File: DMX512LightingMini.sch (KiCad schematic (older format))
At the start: 1 part

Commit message: * 部品配置開始
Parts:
- added C? (x2): C, symbol C
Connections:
- net GND: now reaches IC?.5 (GND)
- net at IC?.6 (A): now also C?.1
- net at IC?.7 (B): now also C?.1
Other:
- moved on the sheet: IC?
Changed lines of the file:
@@
 LIBS:valves
 LIBS:SamacSys_Parts
+LIBS:DMX512LightingMini-cache
 EELAYER 25 0
 EELAYER END
@@
 L ADM4852ARZ-REEL7 IC?
 U 1 1 599C318A
-P 5150 3900
-F 0 "IC?" H 5600 4050 50  0000 C CNN
-F 1 "ADM4852ARZ-REEL7" H 5600 3450 50  0000 C CNN
-F 2 "SOIC127P600X175-8N" H 5600 3350 50  0001 C CNN
-F 3 "" H 5600 3250 50  0001 C CNN
-F 4 "Transceivers" H 5600 3150 50  0001 C CNN "Description"
-F 5 "RS" H 5600 3050 50  0001 C CNN "Supplier_Name"
-F 6 "" H 5600 2950 50  0001 C CNN "RS Part Number"
-F 7 "Analog Devices" H 5600 2850 50  0001 C CNN "Manufacturer_Name"
-F 8 "ADM4852ARZ-REEL7" H 5600 2750 50  0001 C CNN "Manufacturer_Part_Number"
-F 9 "" H 5600 2650 50  0001 C CNN "Allied_Number"
-F 10 "" H 5600 2550 50  0001 C CNN "Other Part Number"
-F 11 "" H 5900 2450 50  0001 C CNN "Height"
-	1    5150 3900
-	1    0    0    -1
+P 5400 3950
+F 0 "IC?" H 5850 4100 50  0000 C CNN
+F 1 "ADM4852ARZ-REEL7" H 5850 3500 50  0000 C CNN
+F 2 "SOIC127P600X175-8N" H 5850 3400 50  0001 C CNN
+F 3 "" H 5850 3300 50  0001 C CNN
+F 4 "Transceivers" H 5850 3200 50  0001 C CNN "Description"
+F 5 "RS" H 5850 3100 50  0001 C CNN "Supplier_Name"
+F 6 "Analog Devices" H 5850 2900 50  0001 C CNN "Manufacturer_Name"
+F 7 "ADM4852ARZ-REEL7" H 5850 2800 50  0001 C CNN "Manufacturer_Part_Number"
+	1    5400 3950
+	-1   0    0    -1
 $EndComp
+$Comp
+L C C?
+U 1 1 599C34D2
+P 3500 4050
+F 0 "C?" H 3525 4150 50  0000 L CNN
+F 1 "C" H 3525 3950 50  0000 L CNN
+F 2 "" H 3538 3900 50  0001 C CNN
+F 3 "" H 3500 4050 50  0001 C CNN
+	1    3500 4050
+	0    1    1    0
+$EndComp
+$Comp
+L C C?
+U 1 1 599C360D
+P 3500 4300
+F 0 "C?" H 3525 4400 50  0000 L CNN
+F 1 "C" H 3525 4200 50  0000 L CNN
+F 2 "" H 3538 4150 50  0001 C CNN
+F 3 "" H 3500 4300 50  0001 C CNN
+	1    3500 4300
+	0    1    1    0
+$EndComp
+$Comp
+L GND #PWR?
+U 1 1 599C37CE
+P 4450 3950
+F 0 "#PWR?" H 4450 3700 50  0001 C CNN
+F 1 "GND" H 4450 3800 50  0000 C CNN
+F 2 "" H 4450 3950 50  0001 C CNN
+F 3 "" H 4450 3950 50  0001 C CNN
+	1    4450 3950
+	0    1    1    0
+$EndComp
+Wire Wire Line
+	4450 3950 4500 3950
+Wire Wire Line
+	4500 4050 3650 4050
+Wire Wire Line
+	3650 4300 3750 4300
+Wire Wire Line
+	3750 4300 3750 4150
+Wire Wire Line
+	3750 4150 4500 4150
 $EndSCHEMATC

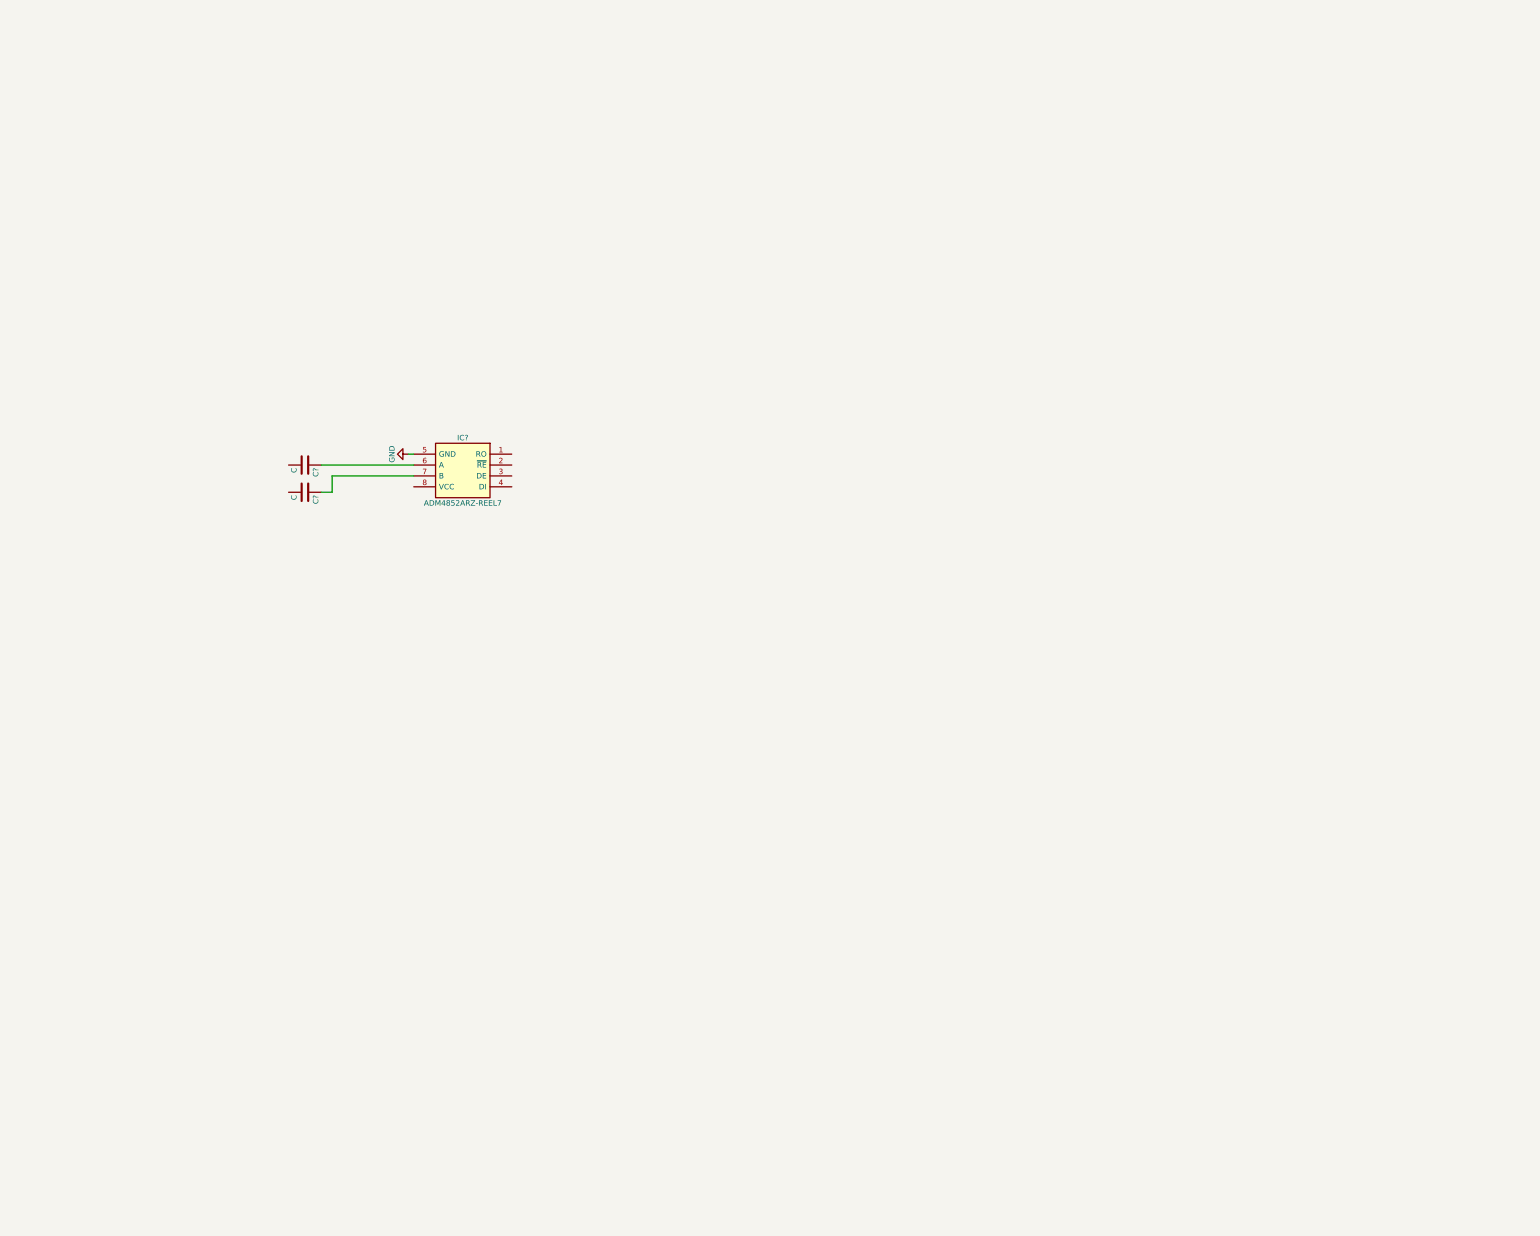
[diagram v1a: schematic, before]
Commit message: * 回路図をほぼ固めた * アートワーク開始
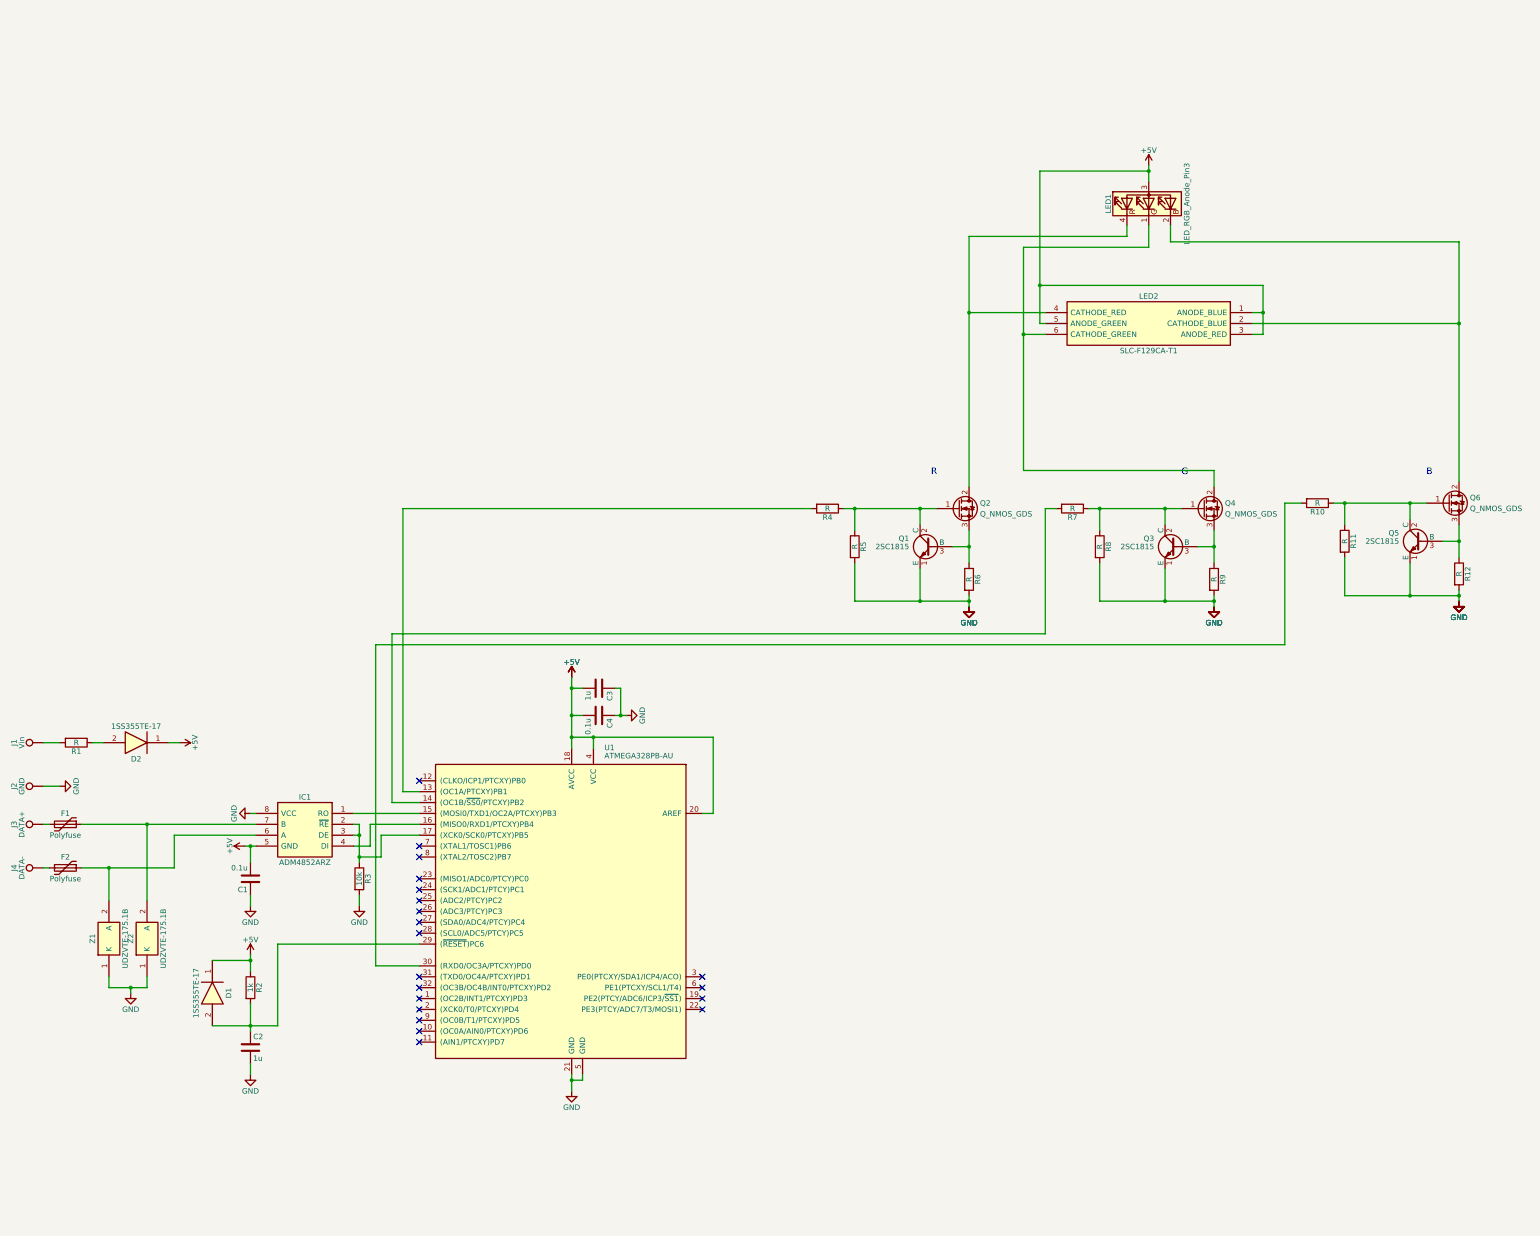
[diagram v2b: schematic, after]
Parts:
- removed C? (x2): C, symbol C
- removed IC?: ADM4852ARZ-REEL7, SOIC127P600X175-8N, symbol ADM4852ARZ-REEL7
- added C1, C4: 0.1u, Capacitors_SMD:C_0603_HandSoldering, symbol C
- added C2, C3: 1u, Capacitors_SMD:C_0603_HandSoldering, symbol C
- added D1, D2: 1SS355TE-17, SODFL2512X90N, symbol 1SS355TE-17
- added F1, F2: Polyfuse, Resistors_SMD:R_1210_HandSoldering, symbol Polyfuse
- added IC1: ADM4852ARZ, SOIC127P600X175-8N, symbol ADM4852ARZ
- added J1: Vin, Wire_Pads:SolderWirePad_single_1-2mmDrill, symbol TEST_1P
- added J2: GND, Wire_Pads:SolderWirePad_single_1-2mmDrill, symbol TEST_1P
- added J3: DATA+, Wire_Pads:SolderWirePad_single_1-2mmDrill, symbol TEST_1P
- added J4: DATA-, Wire_Pads:SolderWirePad_single_1-2mmDrill, symbol TEST_1P
- added LED1: LED_RGB_Anode_Pin3, LEDs:LED_D5.0mm-4, symbol LED_RGB_Anode_Pin3
- added LED2: SLC-F129CA-T1, SLC-F129CA-T1, symbol SLC-F129CA-T1
- added Q1, Q3, Q5: 2SC1815, SOT65P210X90-3N, symbol 2SC1815
- added Q2, Q4, Q6: Q_NMOS_GDS, SOT95P280X100-3N, symbol Q_NMOS_GDS
- added R1, R10, R11, R12, R4, R5, R6, R7, R8, R9: R, Resistors_SMD:R_0603_HandSoldering, symbol R
- added R2: 1k, Resistors_SMD:R_0603_HandSoldering, symbol R
- added R3: 10k, Resistors_SMD:R_0603_HandSoldering, symbol R
- added U1: ATMEGA328PB-AU, Housings_QFP:TQFP-32_7x7mm_Pitch0.8mm, symbol ATMEGA328PB-AU
- added Z1, Z2: UDZVTE-175.1B, UMD2_SOD-323F, symbol UDZVTE-175.1B
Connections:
- net GND: now also C1.1, C2.2, C3.1, C4.1, IC1.8 (VCC), J2.1, Q1.1 (E), Q3.1 (E), Q5.1 (E), R11.2, R12.2, R3.2, R5.2, R6.2, R8.2, R9.2, U1.21 (GND), U1.5 (GND), Z1.1 (K), Z2.1 (K)
- new net: IC1.2 (~RE), IC1.3 (DE), R3.1, U1.17 ((XCK0/SCK0/PTCXY)PB5)
- new net: LED1.2 (BK), LED2.2 (CATHODE_BLUE), Q6.2 (D)
- new net: LED1.4 (RK), LED2.4 (CATHODE_RED), Q2.2 (D)
- new net: LED1.1 (GK), LED2.6 (CATHODE_GREEN), Q4.2 (D)
- new net: R4.2, U1.13 ((OC1A/PTCXY)PB1)
- new net: R7.2, U1.14 ((OC1B/~SS0~/PTCXY)PB2)
- new net: IC1.1 (RO), U1.15 ((MOSI0/TXD1/OC2A/PTCXY)PB3)
- new net: IC1.4 (DI), U1.16 ((MISO0/RXD1/PTCXY)PB4)
- new net: C2.1, D1.2, R2.2, U1.29 ((~RESET~)PC6)
- new net: R10.2, U1.30 ((RXD0/OC3A/PTCXY)PD0)
- new net: Q1.2 (C), Q2.1 (G), R4.1, R5.1
- new net: Q1.3 (B), Q2.3 (S), R6.1
- new net: Q3.2 (C), Q4.1 (G), R7.1, R8.1
- new net: Q3.3 (B), Q4.3 (S), R9.1
- new net: Q5.2 (C), Q6.1 (G), R10.1, R11.1
- new net: Q5.3 (B), Q6.3 (S), R12.1
- new net: J1.1, R1.2
- new net: F1.2, J3.1
- new net: F2.2, J4.1
- new net: F1.1, IC1.7 (B), Z2.2 (A)
- new net: D2.2, R1.1
- new net: F2.1, IC1.6 (A), Z1.2 (A)
- new net +5V: C1.2, C3.2, C4.2, D1.1, D2.1, IC1.5 (GND), LED1.3 (A), LED2.1 (ANODE_BLUE), LED2.3 (ANODE_RED), LED2.5 (ANODE_GREEN), R2.1, U1.18 (AVCC), U1.20 (AREF), U1.4 (VCC)
- no-connect marks 0 -> 20
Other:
- note added: "B"
- note added: "G"
- note added: "R"

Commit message: * アートワーク作業中
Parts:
- added C5: 10u, Capacitors_SMD:C_0805_HandSoldering, symbol C
- added J10: GND, Measurement_Points:Measurement_Point_Square-SMD-Pad_Small, symbol TEST_1P
- added J5: RESET, Measurement_Points:Measurement_Point_Square-SMD-Pad_Small, symbol TEST_1P
- added J6: MOSI, Measurement_Points:Measurement_Point_Square-SMD-Pad_Small, symbol TEST_1P
- added J7: MISO, Measurement_Points:Measurement_Point_Square-SMD-Pad_Small, symbol TEST_1P
- added J8: SCK, Measurement_Points:Measurement_Point_Square-SMD-Pad_Small, symbol TEST_1P
- added J9: Vcc, Measurement_Points:Measurement_Point_Square-SMD-Pad_Small, symbol TEST_1P
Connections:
- net +5V: now also C5.1, J9.1
- net GND: now also C5.2, J10.1
- net at IC1.2 (~RE), IC1.3 (DE), R3.1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: now also J8.1
- net at IC1.1 (RO), U1.15 ((MOSI0/TXD1/OC2A/PTCXY)PB3): now also J6.1
- net at IC1.4 (DI), U1.16 ((MISO0/RXD1/PTCXY)PB4): now also J7.1
- net at C2.1, D1.2, R2.2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: now also J5.1
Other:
- moved on the sheet: C2, D1

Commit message: * アートワーク完了    * 四角版
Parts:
- removed C5: 10u, Capacitors_SMD:C_0805_HandSoldering, symbol C
- removed D1, D2: 1SS355TE-17, SODFL2512X90N, symbol 1SS355TE-17
- removed F1, F2: Polyfuse, Resistors_SMD:R_1210_HandSoldering, symbol Polyfuse
- removed IC1: ADM4852ARZ, SOIC127P600X175-8N, symbol ADM4852ARZ
- removed J1: Vin, Wire_Pads:SolderWirePad_single_1-2mmDrill, symbol TEST_1P
- removed J10: GND, Measurement_Points:Measurement_Point_Square-SMD-Pad_Small, symbol TEST_1P
- removed J2: GND, Wire_Pads:SolderWirePad_single_1-2mmDrill, symbol TEST_1P
- removed J3: DATA+, Wire_Pads:SolderWirePad_single_1-2mmDrill, symbol TEST_1P
- removed J4: DATA-, Wire_Pads:SolderWirePad_single_1-2mmDrill, symbol TEST_1P
- removed J5: RESET, Measurement_Points:Measurement_Point_Square-SMD-Pad_Small, symbol TEST_1P
- removed J6: MOSI, Measurement_Points:Measurement_Point_Square-SMD-Pad_Small, symbol TEST_1P
- removed J7: MISO, Measurement_Points:Measurement_Point_Square-SMD-Pad_Small, symbol TEST_1P
- removed J8: SCK, Measurement_Points:Measurement_Point_Square-SMD-Pad_Small, symbol TEST_1P
- removed J9: Vcc, Measurement_Points:Measurement_Point_Square-SMD-Pad_Small, symbol TEST_1P
- removed LED1: LED_RGB_Anode_Pin3, LEDs:LED_D5.0mm-4, symbol LED_RGB_Anode_Pin3
- removed LED2: SLC-F129CA-T1, SLC-F129CA-T1, symbol SLC-F129CA-T1
- removed Q1, Q3, Q5: 2SC1815, SOT65P210X90-3N, symbol 2SC1815
- removed Q2, Q4, Q6: Q_NMOS_GDS, SOT95P280X100-3N, symbol Q_NMOS_GDS
- removed R10, R11, R12, R7, R8, R9: R, Resistors_SMD:R_0603_HandSoldering, symbol R
- removed U1: ATMEGA328PB-AU, Housings_QFP:TQFP-32_7x7mm_Pitch0.8mm, symbol ATMEGA328PB-AU
- removed Z1, Z2: UDZVTE-175.1B, UMD2_SOD-323F, symbol UDZVTE-175.1B
- added D1: L-154A4SURKQBDZGW, KNIGHTBRIGHT-1.27PITCH-4PIN, symbol L-154A4SURKQBDZGW
- added IC1: PIC12F1840-I_SN, SOIC127P600X175-8N, symbol PIC12F1840-I_SN
- added IC2: ADM4852ARZ, SOIC127P600X175-8N, symbol ADM4852ARZ
- added TP1: +5V, Wire_Pads:SolderWirePad_single_1-2mmDrill, symbol TEST
- added TP2: DATA+, Wire_Pads:SolderWirePad_single_1-2mmDrill, symbol TEST
- added TP3: DATA-, Wire_Pads:SolderWirePad_single_1-2mmDrill, symbol TEST
- added TP4: GND, Wire_Pads:SolderWirePad_single_1-2mmDrill, symbol TEST
- C3: value 1u -> 0.1u
- R1: value R -> 10k
- R2: value 1k -> 100
- R3: value 10k -> 100
- R4, R5, R6: value R -> 330
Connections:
- net +5V: now also C2.1, C3.1, C4.1, R1.1, IC1.1 (VDD), IC2.8 (VCC), TP1.1; no longer C1.2, C3.2, C4.2, R2.1
- net GND: now also C1.2, C3.2, C4.2, IC1.8 (VSS), IC2.2 (~RE), IC2.3 (DE), IC2.4 (DI), IC2.5 (GND), TP4.1; no longer C1.1, C3.1, C4.1, R3.2, R5.2, R6.2
- net at R3.1: now also TP3.1
- net at R4.2: now also D1.4 (GREEN)
- net DATA+: now reaches R2.2
- net DATA+: now also IC2.7 (B); no longer C2.1
- net at R4.1: now also IC1.3 (RA4); no longer R5.1
- net at R6.1: now also IC1.7 (RA0/ICSPDAT)
- net at R1.2: now also C1.1, IC1.4 (~MCLR~/VPP/RA3)
- new net: IC1.2 (RA5), R5.2
- new net: D1.2, IC1.5 (RA2)
- new net: IC1.6 (RA1/ICSPCLK), IC2.1 (RO)
- new net: D1.1 (RED), R6.2
- new net: D1.3 (BLUE), R5.1
- new net DATA-: IC2.6 (A), R3.2
- no-connect marks 20 -> 0
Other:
- note removed: "B"
- note removed: "G"
- note removed: "R"
